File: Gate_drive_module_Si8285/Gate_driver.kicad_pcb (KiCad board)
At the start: 2 copper layers, 96.7 x 50 mm, 38 parts, among them J1 CONN_01X10, J2 CONN_01X04, J3 CONN_01X03, J4 CONN_01X03, J5 CONN_01X03, U1 Si8285, U2 Mornsun_QA01C

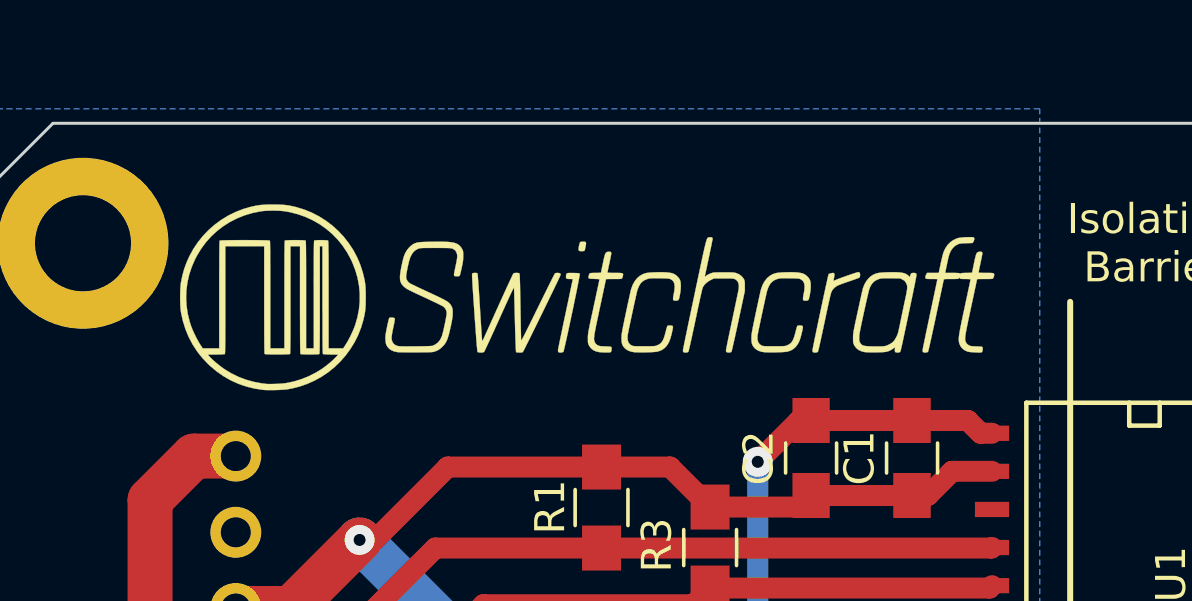
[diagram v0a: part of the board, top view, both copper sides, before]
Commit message: Adjusted Switchcraft logo position
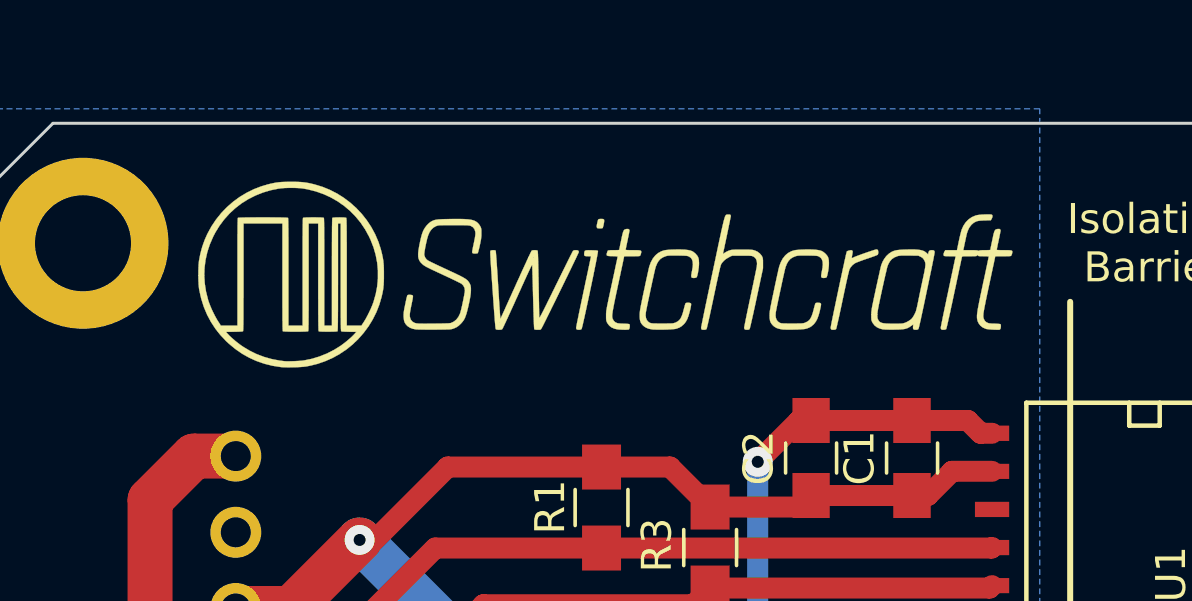
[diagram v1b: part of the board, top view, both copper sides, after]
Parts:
- moved G*** 0.97 mm to (117.6, 111.0)
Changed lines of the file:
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@@
   )
   (layers
-    (0 F.Cu signal hide)
-    (31 B.Cu signal hide)
-    (32 B.Adhes user hide)
-    (33 F.Adhes user hide)
+    (0 F.Cu signal)
+    (31 B.Cu signal)
+    (32 B.Adhes user)
+    (33 F.Adhes user)
     (34 B.Paste user)
-    (35 F.Paste user hide)
+    (35 F.Paste user)
     (36 B.SilkS user)
     (37 F.SilkS user)
-    (38 B.Mask user hide)
-    (39 F.Mask user hide)
-    (40 Dwgs.User user hide)
-    (41 Cmts.User user hide)
-    (42 Eco1.User user hide)
-    (43 Eco2.User user hide)
-    (44 Edge.Cuts user hide)
+    (38 B.Mask user)
+    (39 F.Mask user)
+    (40 Dwgs.User user)
+    (41 Cmts.User user)
+    (42 Eco1.User user)
+    (43 Eco2.User user)
+    (44 Edge.Cuts user)
     (45 Margin user)
-    (46 B.CrtYd user hide)
+    (46 B.CrtYd user)
     (47 F.CrtYd user)
     (48 B.Fab user)
-    (49 F.Fab user hide)
+    (49 F.Fab user)
   )
   (setup
@@
     (aux_axis_origin 95 156)
     (grid_origin 95 156)
-    (visible_elements FFFEC061)
+    (visible_elements FFFFFFFF)
     (pcbplotparams
       (layerselection 0x00030_80000001)
@@
   )
   (module Switchcraft:Switchcraft_medium_logo (layer F.Cu)
-    (at 117 111.8)
+    (at 117.606 111.042)
     (fp_text reference G*** (at 0 3.5) (layer F.SilkS) hide
       (effects (font (thickness 0.3)))

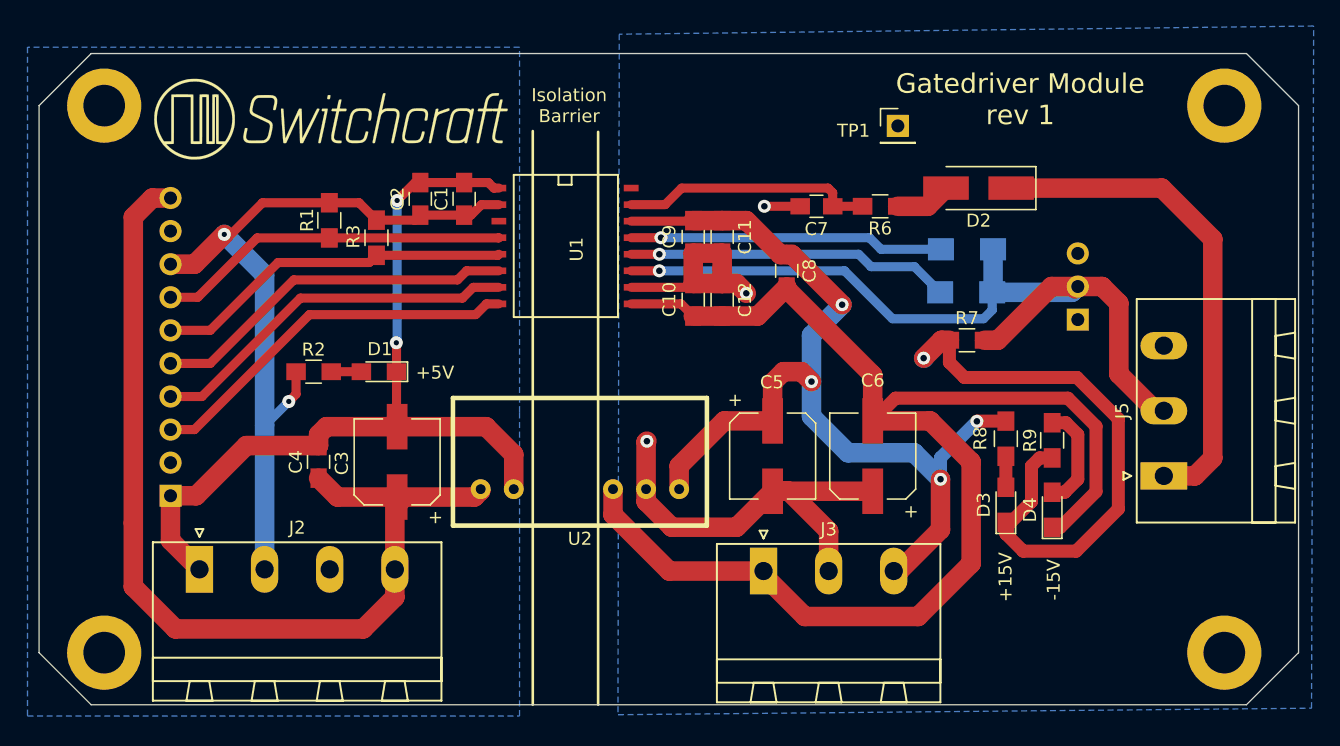
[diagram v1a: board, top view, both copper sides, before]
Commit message: Moved some footprints
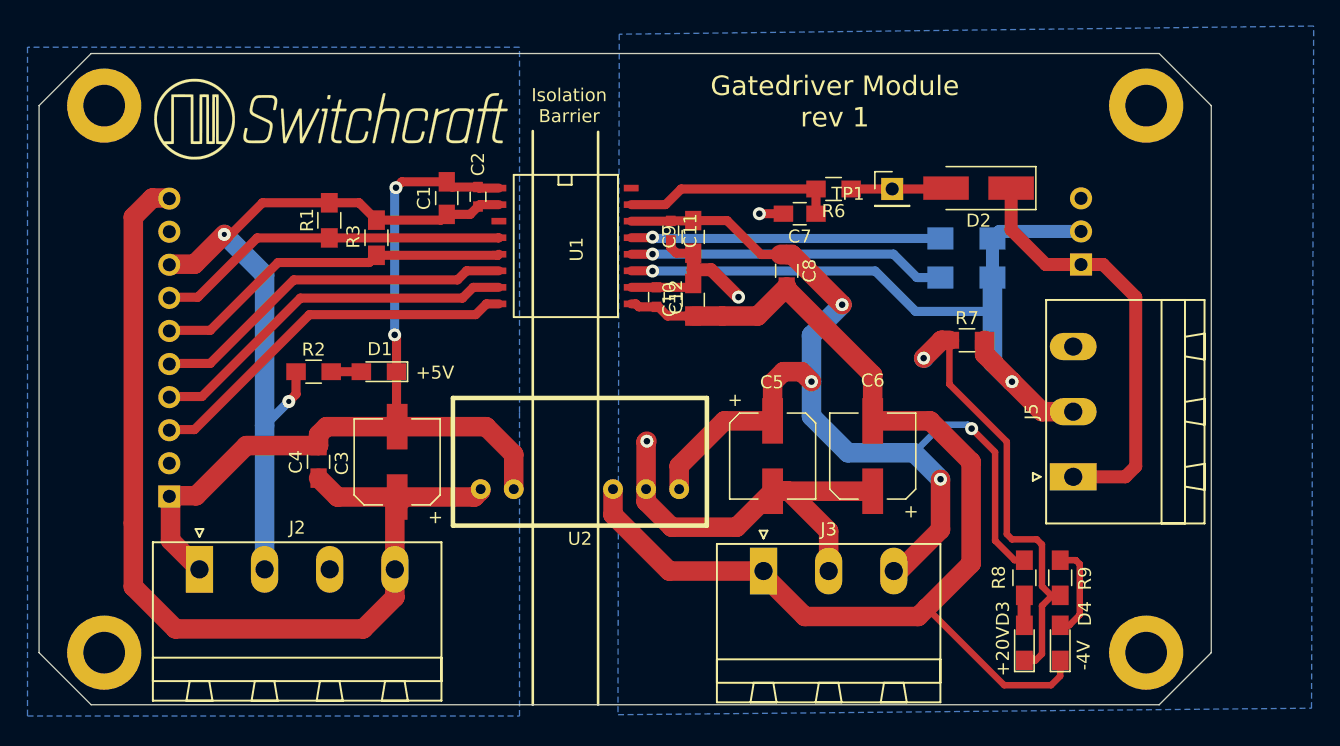
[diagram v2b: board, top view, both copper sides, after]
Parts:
- C11, C12, C2: footprint Capacitors_SMD:C_0805_HandSoldering -> Capacitors_SMD:C_0603
- moved R8 10.8 mm to (170.7, 146.2)
- moved D3 10.7 mm to (170.7, 151.2)
- moved R9 10.6 mm to (173.4, 146.2)
- moved D4 10.2 mm to (173.4, 151.2)
- moved J5 6.96 mm to (174.4, 138.5)
- moved REF** 6.00 mm to (180.0, 110.0)
- moved REF** 6.00 mm to (180.0, 152.0)
- moved C12 5.05 mm to (142.4, 124.7)
- moved TP1 4.86 mm to (160.5, 116.4)
- moved C2 4.43 mm to (128.7, 117.0)
- moved J4 4.24 mm to (175.0, 122.2)
- moved C11 3.98 mm to (143.5, 119.6)
- moved R6 3.81 mm to (156.0, 116.4)
- moved C7 1.41 mm to (153.4, 118.3)
- moved C1 1.34 mm to (126.3, 117.1)
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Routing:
- net VEE_ISO: track 105.8 -> 91.7 mm
- net GND_ISO: track 96.1 -> 84.1 mm
- net VCC_ISO: track 75.1 -> 85.5 mm
- net Net-(D2-Pad1): track 38.2 -> 33.0 mm
- net Net-(J4-Pad2): track 63.8 -> 59.7 mm, vias 1 -> 2
- net Net-(D2-Pad2): track 4.29 -> 7.31 mm
- net Net-(C7-Pad1): track 19.5 -> 16.6 mm
- net Net-(D4-Pad2): track 8.16 -> 7.36 mm
- net GND: track 65.1 -> 65.9 mm
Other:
- board size 96.7 x 50 mm -> 90 x 50 mm
- board text added: "+20V"
- board text added: "-4V"
- board text added: "Don't blame me. I'm an interpreter. I'm not supposed to know a power socket from a computer terminal."
- board text removed: "+15V"
- board text removed: "-15V"

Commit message: Added open hardware logo
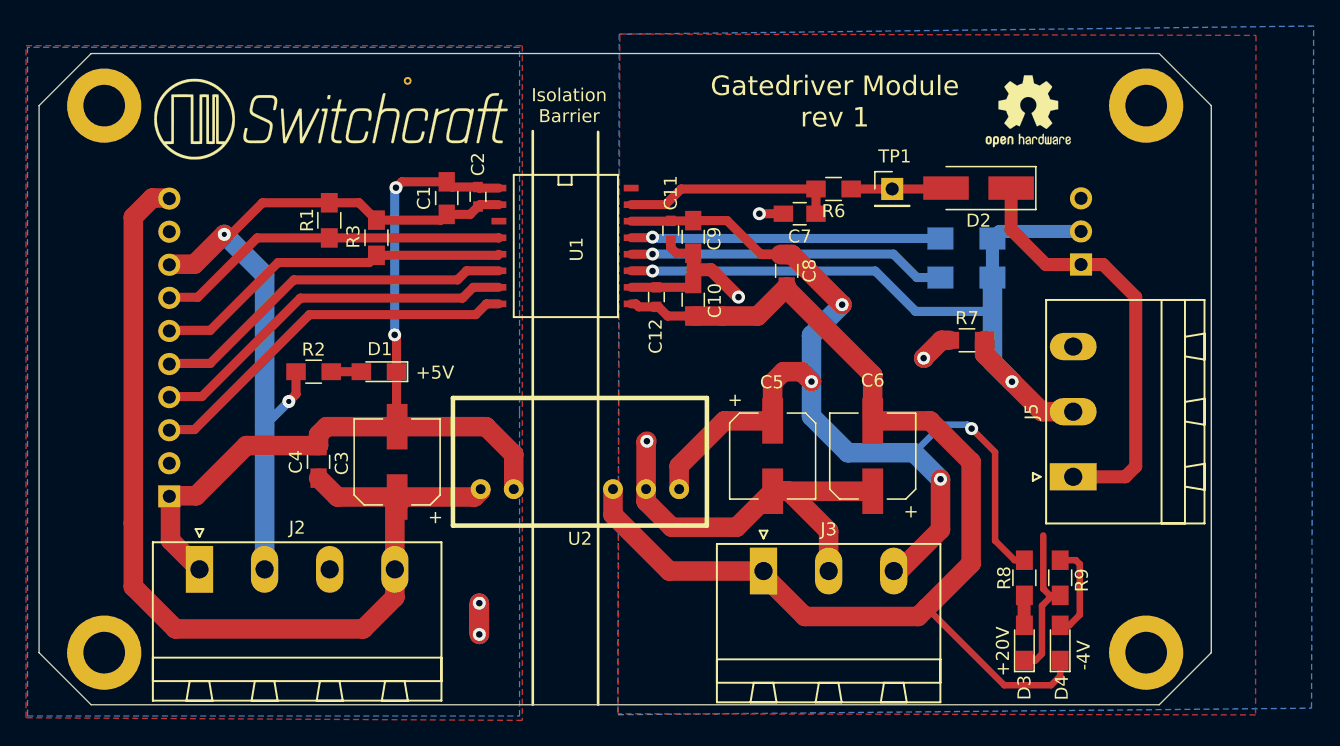
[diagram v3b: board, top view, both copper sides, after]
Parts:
- added REF**: VIA-0.6mm, VIA:VIA-0.6mm, F.Cu at (123.3, 108.1)
- added REF***: OSHW-Logo2_7.3x6mm_SilkScreen, Symbols:OSHW-Logo2_7.3x6mm_SilkScreen, F.Cu at (170.9, 110.4)
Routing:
- net GND_ISO: track 84.1 -> 65.1 mm
- net (no net): track 0.00 -> 4.80 mm, vias 0 -> 2
- added copper zone on F.Cu, net GND
- added copper zone on F.Cu, net GND_ISO
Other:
- net class Default: trace_width 1.5 -> 0.5
- rule trace_min: 0.2 -> 0.5
- board text added: "https://www.switchcraft.org/"

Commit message: Minor cosmetic changes
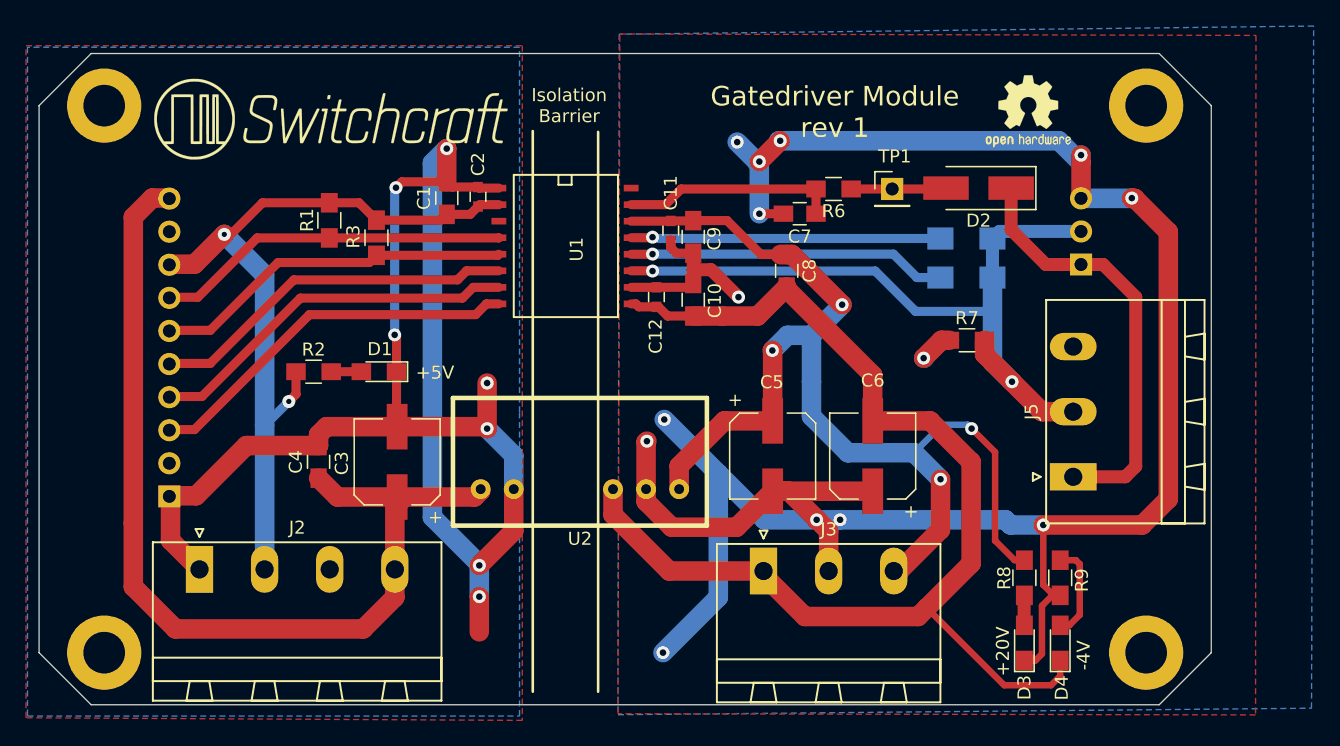
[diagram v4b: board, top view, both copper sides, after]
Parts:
- removed the REF** at (123.3, 108.1)
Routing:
- net GND_ISO: track 65.1 -> 189.0 mm, vias 4 -> 14
- net GND: track 65.9 -> 118.1 mm, vias 2 -> 7
- net (no net): track 4.80 -> 0.00 mm, vias 2 -> 0
- net VCC_ISO: track 85.5 -> 87.8 mm
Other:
- net class Default: trace_width 0.5 -> 1.5

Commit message: Added some PCB annotations
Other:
- board text added: "+15 V"
- board text added: "-15 V"
- board text added: "DRAIN"
- board text added: "GATE"
- board text added: "GND"
- board text added: "NC"
- board text added: "RDY"
- board text added: "SOURCE"
- board text added: "SRC"
- board text added: "VCC"
- board text added: "VIN+"
- board text added: "VIN-"
- board text added: "~FLT"
- board text added: "~RST"
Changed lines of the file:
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@@
     (area 94.949999 105.949999 185.050001 156.050001)
     (thickness 1.6)
-    (drawings 26)
+    (drawings 42)
     (tracks 306)
     (zones 0)
@@
   )
   (layers
-    (0 F.Cu signal hide)
+    (0 F.Cu signal)
     (31 B.Cu signal)
     (32 B.Adhes user)
@@
     (descr "Through hole straight pin header, 1x03, 2.54mm pitch, single row")
     (tags "Through hole pin header THT 1x03 2.54mm single row")
-    (fp_text reference J4 (at 2.9 -2.9) (layer B.SilkS)
+    (fp_text reference J4 (at -3 1.55) (layer B.SilkS)
       (effects (font (size 1 1) (thickness 0.15)) (justify mirror))
     )
@@
       (xy -0.113933 -2.757629) (xy -0.013056 -2.757714) (xy 0 -2.757714) (xy 0.10391 -2.757652)) (layer F.SilkS) (width 0.01))
   )
+  (gr_text SOURCE (at 180.75 138.5) (layer B.SilkS)
+    (effects (font (size 1 1) (thickness 0.2)) (justify mirror))
+  )
+  (gr_text GATE (at 180.75 133.25) (layer B.SilkS)
+    (effects (font (size 1 1) (thickness 0.2)) (justify mirror))
+  )
+  (gr_text DRAIN (at 180.75 128.5) (layer B.SilkS)
+    (effects (font (size 1 1) (thickness 0.2)) (justify mirror))
+  )
+  (gr_text DRAIN (at 181 122.5) (layer F.SilkS)
+    (effects (font (size 1 1) (thickness 0.2)))
+  )
+  (gr_text GATE (at 181.25 119.75) (layer F.SilkS)
+    (effects (font (size 1 1) (thickness 0.2)))
+  )
+  (gr_text SRC (at 181.5 117.25) (layer F.SilkS)
+    (effects (font (size 1 1) (thickness 0.2)))
+  )
+  (gr_text NC (at 101.25 137.25) (layer F.SilkS)
+    (effects (font (size 1 1) (thickness 0.2)))
+  )
+  (gr_text GND (at 101.25 140) (layer F.SilkS)
+    (effects (font (size 1 1) (thickness 0.2)))
+  )
+  (gr_text VIN- (at 101.25 134.75) (layer F.SilkS)
+    (effects (font (size 1 1) (thickness 0.2)))
+  )
+  (gr_text VIN+ (at 101.25 132.25) (layer F.SilkS)
+    (effects (font (size 1 1) (thickness 0.2)))
+  )
+  (gr_text RDY (at 101.5 129.75) (layer F.SilkS)
+    (effects (font (size 1 1) (thickness 0.2)))
+  )
+  (gr_text ~FLT (at 101.5 127.25) (layer F.SilkS)
+    (effects (font (size 1 1) (thickness 0.2)))
+  )
+  (gr_text ~RST (at 101.5 124.5) (layer F.SilkS)
+    (effects (font (size 1 1) (thickness 0.2)))
+  )
+  (gr_text "-15 V" (at 100.5 119.75) (layer F.SilkS)
+    (effects (font (size 1 1) (thickness 0.2)))
+  )
+  (gr_text "+15 V" (at 100.5 117.25) (layer F.SilkS)
+    (effects (font (size 1 1) (thickness 0.2)))
+  )
+  (gr_text VCC (at 101.4 122.2) (layer F.SilkS)
+    (effects (font (size 1 1) (thickness 0.2)))
+  )
   (gr_line (start 137.922 155) (end 137.922 107) (angle 90) (layer B.SilkS) (width 0.2))

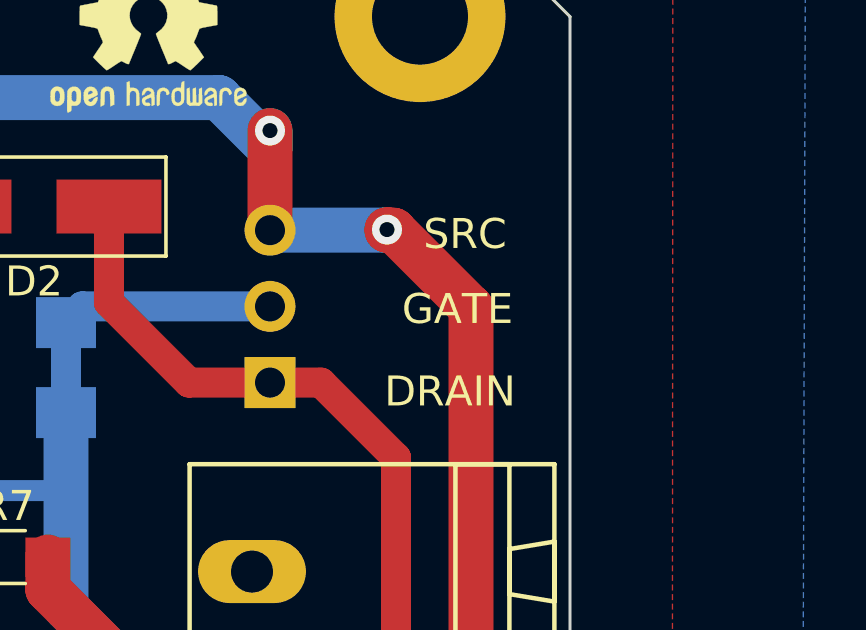
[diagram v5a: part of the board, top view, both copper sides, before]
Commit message: Minor silkscreen change
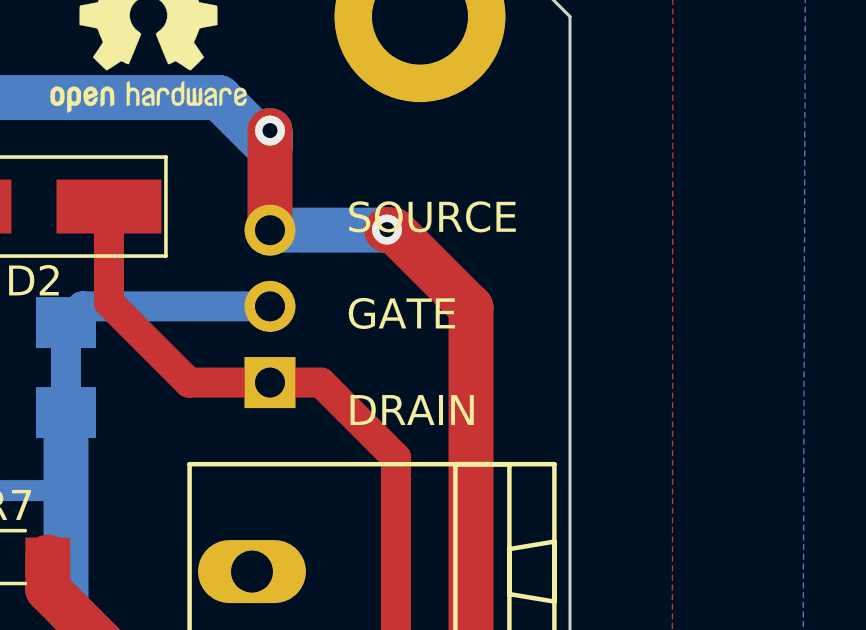
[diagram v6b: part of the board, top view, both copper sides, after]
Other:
- board text added: "SOURCE GATE DRAIN"
- board text removed: "SRC"
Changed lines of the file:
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@@
     (links 70)
     (no_connects 0)
-    (area 94.949999 105.949999 185.050001 156.050001)
+    (area 84.450001 94.6 203.43 163.500001)
     (thickness 1.6)
-    (drawings 42)
+    (drawings 40)
     (tracks 306)
     (zones 0)
@@
     (effects (font (size 1 1) (thickness 0.2)) (justify mirror))
   )
-  (gr_text DRAIN (at 181 122.5) (layer F.SilkS)
-    (effects (font (size 1 1) (thickness 0.2)))
-  )
-  (gr_text GATE (at 181.25 119.75) (layer F.SilkS)
-    (effects (font (size 1 1) (thickness 0.2)))
-  )
-  (gr_text SRC (at 181.5 117.25) (layer F.SilkS)
-    (effects (font (size 1 1) (thickness 0.2)))
+  (gr_text "SOURCE\n\nGATE\n\nDRAIN" (at 177.55 119.932) (layer F.SilkS)
+    (effects (font (size 1 1) (thickness 0.2)) (justify left))
   )
   (gr_text NC (at 101.25 137.25) (layer F.SilkS)
